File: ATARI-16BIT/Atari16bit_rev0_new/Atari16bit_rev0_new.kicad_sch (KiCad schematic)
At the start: 10 parts, among them J1 ACSI (IDC-20), J2 SD Card module, U1 74LS641, U2 74LS641, U3 74LS641, U4 ESP32-DevKitC

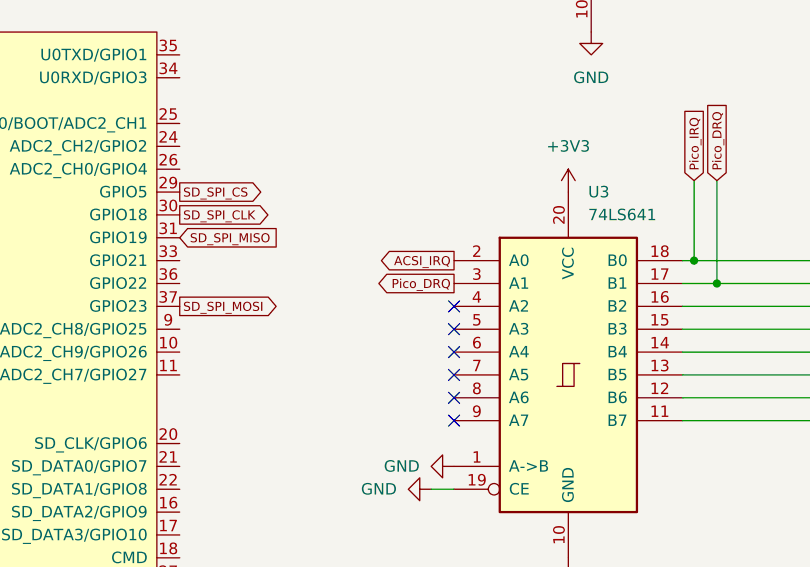
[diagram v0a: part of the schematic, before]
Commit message: Fixed signal label error ACSI_DRQ
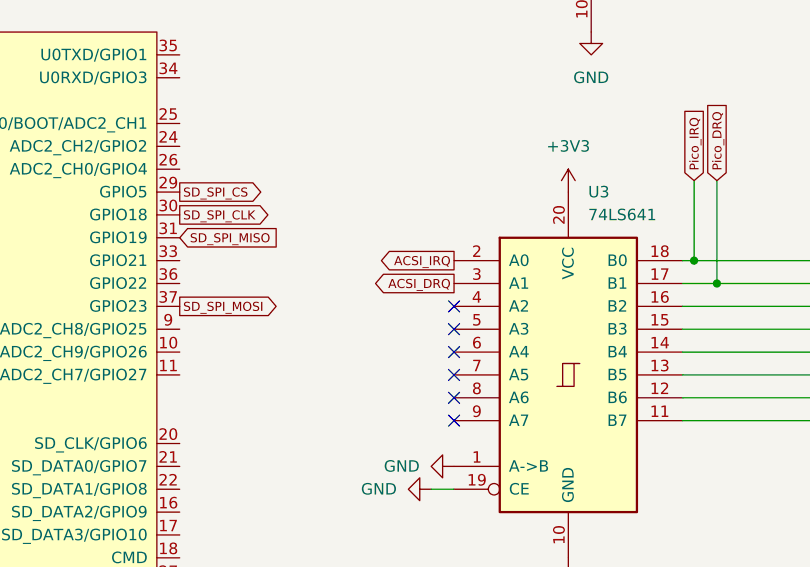
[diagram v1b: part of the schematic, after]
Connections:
- net ACSI_DRQ: now also U3.3 (A1)
- net Pico_DRQ: no longer U3.3 (A1)
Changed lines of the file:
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@@
 		)
 	)
-	(global_label "Pico_DRQ"
+	(global_label "ACSI_DRQ"
 		(shape output)
 		(at 129.54 156.21 180)
@@
 		)
 		(property "Intersheetrefs" "${INTERSHEET_REFS}"
-			(at 120.1421 156.21 0)
+			(at 120.0945 156.21 0)
 			(effects
 				(font

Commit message: Schematic now passes ERC
Added PWR_FLAG
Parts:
- J1: footprint (none) -> Connector_IDC:IDC-Header_2x10_P2.54mm_Vertical
- J2: footprint (none) -> Connector_PinHeader_2.54mm:PinHeader_1x06_P2.54mm_Vertical
- U1, U2, U3: footprint (none) -> Package_DIP:CERDIP-20_W7.62mm_SideBrazed
- U4: footprint PCM_Espressif:ESP32-DevKitC -> esp:ESP32-DevKitC
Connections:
- net +3V3 is gone; now on net +3.3V: RN2.1 (common), U2.1 (A->B), U3.20 (VCC)
- net ACSI_DO is gone; now on net ACSI_D0: J1.1 (Pin_1)
- net +3.3V: now also A1.39 (VSYS)
- no-connect marks 10 -> 46
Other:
- moved on the sheet: RN1, RN3, U1, U3

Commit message: [Atari16bit] Schematic update
pcb WIP
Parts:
- A1: footprint Module_RaspberryPi_Pico:RaspberryPi_Pico_Common -> pico:RaspberryPi_Pico_Common_THT
- J1: footprint Connector_IDC:IDC-Header_2x10_P2.54mm_Vertical -> ACSI:Connector_ACSI_IDC
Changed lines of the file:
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@@
 			)
 		)
-		(property "Footprint" "Module_RaspberryPi_Pico:RaspberryPi_Pico_Common"
+		(property "Footprint" "pico:RaspberryPi_Pico_Common_THT"
 			(at 64.77 20.32 0)
 			(effects
@@
 			)
 		)
-		(property "Footprint" "Connector_IDC:IDC-Header_2x10_P2.54mm_Vertical"
+		(property "Footprint" "ACSI:Connector_ACSI_IDC"
 			(at 142.24 217.17 0)
 			(effects

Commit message: [Atari16bit] Updates
Updated: Pins of Pico, Added UART from pico to esp32 and added 5V pullup on databus.
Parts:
- added RN4: 10k, Resistor_THT:R_Array_SIP9, symbol Device:R_Network08
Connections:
- net ACSI_D0: now also RN4.9 (R8)
- net ACSI_D1: now also RN4.8 (R7)
- net ACSI_D2: now also RN4.7 (R6)
- net ACSI_D3: now also RN4.6 (R5)
- net ACSI_D4: now also RN4.5 (R4)
- net ACSI_D5: now also RN4.4 (R3)
- net ACSI_D6: now also RN4.3 (R2)
- net ACSI_D7: now also RN4.2 (R1)
- net DDIR: now also A1.10 (GPIO7); no longer A1.7 (GPIO5)
- net Pico_DRQ: now also A1.5 (GPIO3); no longer A1.6 (GPIO4)
- net ESP_UART_RX: now reaches U4.27 (GPIO16)
- net ESP_UART_RX: now also A1.6 (GPIO4)
- net ESP_UART_TX: now reaches U4.28 (GPIO17)
- net ESP_UART_TX: now also A1.7 (GPIO5)
- new net +5V: RN4.1 (common)
- no-connect marks 46 -> 42
